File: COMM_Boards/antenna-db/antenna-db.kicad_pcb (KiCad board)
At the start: 4 copper layers, 95 x 95 mm, 65 parts, among them J1 Conn_01x03, J2 Conn_01x04, J3 Conn_01x02_Male, J6 Conn_01x02_Male, T1 MABA-007159-000000, T2 MABA-007159-000000, U1 SC4216HSETRT, U2 STM32F030CCT6, U3 SC4216HSETRT, U4 74AHC1G08, U5 74AHC1G08

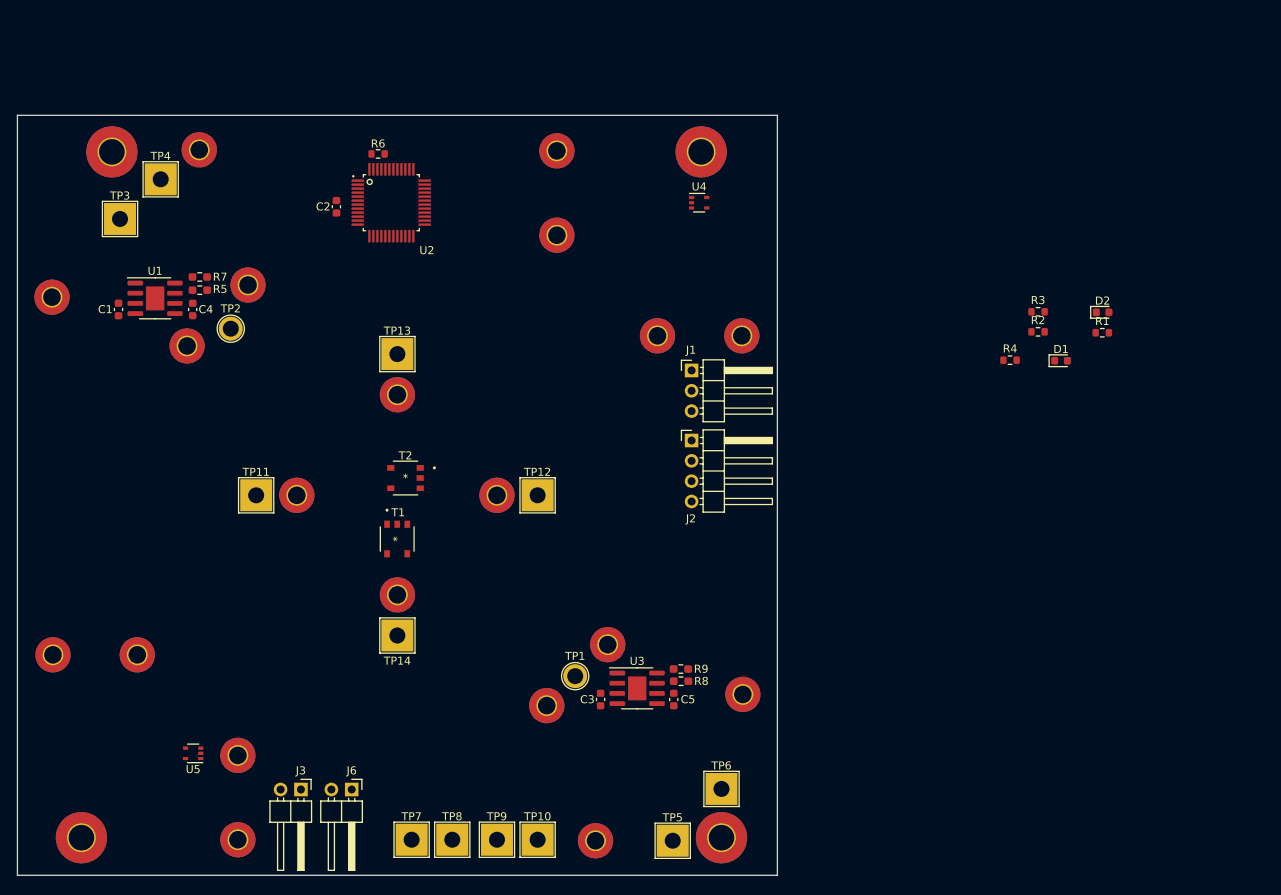
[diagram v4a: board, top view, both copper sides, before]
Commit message: finish layout of ANTT-DBD
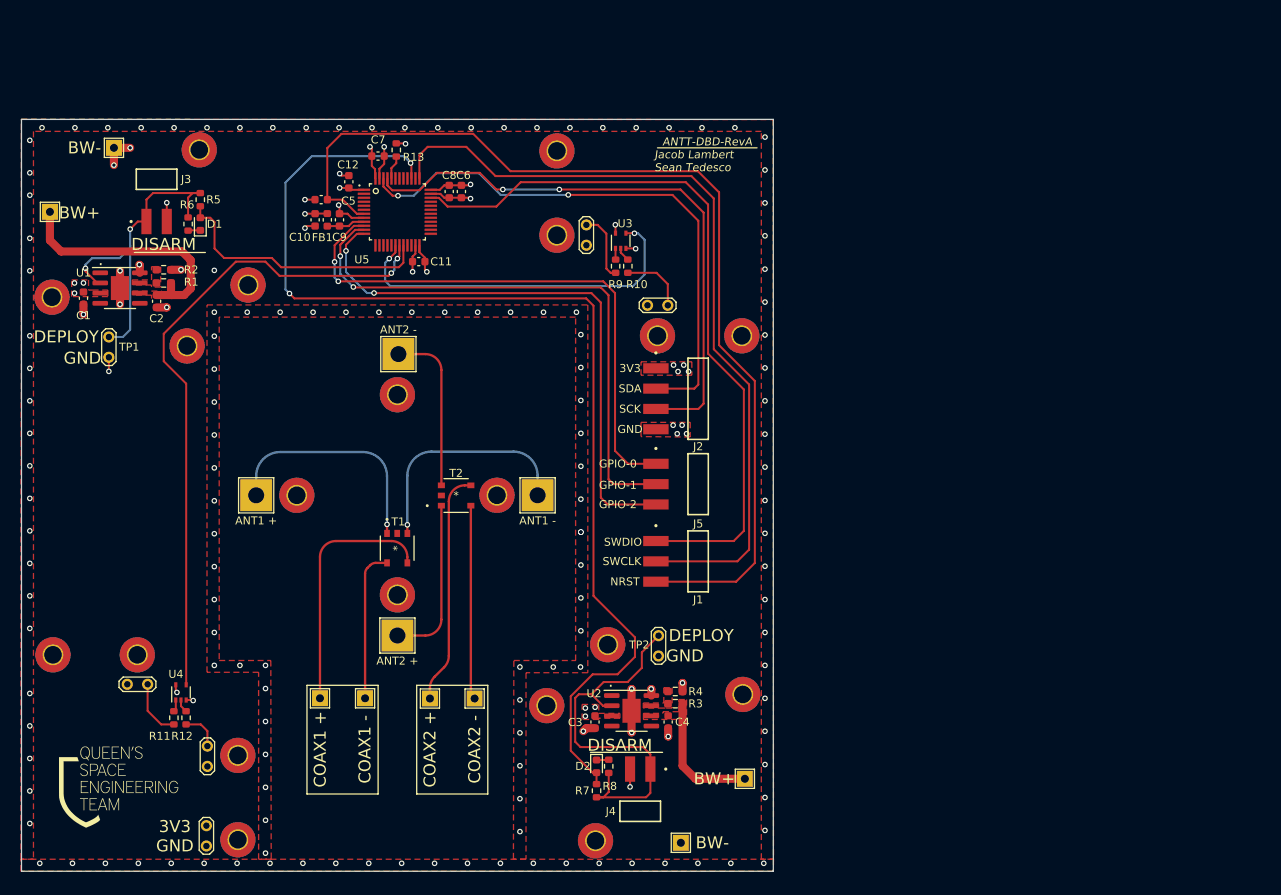
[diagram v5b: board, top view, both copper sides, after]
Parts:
- removed H1, H2, H3, H4: MountingHole_Pad, MountingHole:MountingHole_3.2mm_M3_Pad_TopBottom
- removed J6: Conn_01x02_Male, Connector_PinHeader_2.54mm:PinHeader_1x02_P2.54mm_Horizontal
- added C10: 10u, Capacitor_SMD:C_0603_1608Metric, F.Cu at (146.6, 60.9)
- added C11: 100n, Capacitor_SMD:C_0603_1608Metric, F.Cu at (159.5, 66.2)
- added C12: 100n, Capacitor_SMD:C_0603_1608Metric, F.Cu at (150.8, 56.2)
- added C6: 10u, Capacitor_SMD:C_0603_1608Metric, F.Cu at (164.8, 57.4)
- added C7: 100n, Capacitor_SMD:C_0603_1608Metric, F.Cu at (154.4, 53.0)
- added C8: 100n, Capacitor_SMD:C_0603_1608Metric, F.Cu at (163.3, 57.4)
- added C9: 100n, Capacitor_SMD:C_0603_1608Metric, F.Cu at (149.6, 60.9)
- added FB1: 100R @ 100M, Inductor_SMD:L_0603_1608Metric, F.Cu at (148.1, 60.9)
- added G***: LOGO, LOGO, F.Cu at (122.0, 131.7)
- added J4: Conn_01x02_Male, qset-footprints:SAMTEC_TSM-102-01-L-SH, F.Cu at (187.2, 134.9)
- added J5: Conn_01x03, qset-footprints:SAMTEC_TSM-103-01-L-SH, F.Cu at (194.4, 94.0)
- added R10: 0, Resistor_SMD:R_0603_1608Metric, F.Cu at (185.6, 66.7)
- added R11: 0, Resistor_SMD:R_0603_1608Metric, F.Cu at (128.9, 123.2)
- added R12: 0, Resistor_SMD:R_0603_1608Metric, F.Cu at (130.4, 123.2)
- added R9: 0, Resistor_SMD:R_0603_1608Metric, F.Cu at (184.1, 66.7)
- added TP3: Power Sensing, TestPoint:TestPoint_2Pads_Pitch2.54mm_Drill0.8mm, F.Cu at (133.0, 136.7)
- added TP4: TestPoint_2Pole, TestPoint:TestPoint_2Pads_Pitch2.54mm_Drill0.8mm, F.Cu at (180.5, 64.1)
- added TP5: TestPoint_2Pole, TestPoint:TestPoint_2Pads_Pitch2.54mm_Drill0.8mm, F.Cu at (188.1, 71.6)
- added TP6: TestPoint_2Pole, TestPoint:TestPoint_2Pads_Pitch2.54mm_Drill0.8mm, F.Cu at (123.1, 119.0)
- added TP7: TestPoint_2Pole, TestPoint:TestPoint_2Pads_Pitch2.54mm_Drill0.8mm, F.Cu at (133.1, 129.3)
- J1: footprint Connector_PinHeader_2.54mm:PinHeader_1x03_P2.54mm_Horizontal -> qset-footprints:SAMTEC_TSM-103-01-L-SH
- J2: footprint Connector_PinHeader_2.54mm:PinHeader_1x04_P2.54mm_Horizontal -> qset-footprints:SAMTEC_TSM-104-01-L-SH
- J3: footprint Connector_PinHeader_2.54mm:PinHeader_1x02_P2.54mm_Horizontal -> qset-footprints:SAMTEC_TSM-102-01-L-SH
- TP1: value PWR_EN_144 -> Manual Enable - 144 Deployment; footprint TestPoint:TestPoint_Plated_Hole_D2.0mm -> TestPoint:TestPoint_2Pads_Pitch2.54mm_Drill0.8mm
- TP10: renamed from TP11; value 144 Atenna Arm + -> ANT1 +
- TP11: renamed from TP12; value 144 Atenna Arm - -> ANT1 -
- TP12: renamed from TP9; footprint TestPoint:TestPoint_THTPad_4.0x4.0mm_Drill2.0mm -> TestPoint:TestPoint_THTPad_2.0x2.0mm_Drill1.0mm
- TP13: renamed from TP10; footprint TestPoint:TestPoint_THTPad_4.0x4.0mm_Drill2.0mm -> TestPoint:TestPoint_THTPad_2.0x2.0mm_Drill1.0mm
- TP14: renamed from TP13; value 434 Atenna Arm + -> ANT2 +
- TP15: renamed from TP14; value 434 Atenna Arm - -> ANT2 -
- TP16: renamed from TP3; value TestPoint -> 144 Burn Wire -; footprint TestPoint:TestPoint_THTPad_4.0x4.0mm_Drill2.0mm -> TestPoint:TestPoint_THTPad_2.0x2.0mm_Drill1.0mm
- TP17: renamed from TP4; value TestPoint -> 144 Burn Wire +; footprint TestPoint:TestPoint_THTPad_4.0x4.0mm_Drill2.0mm -> TestPoint:TestPoint_THTPad_2.0x2.0mm_Drill1.0mm
- TP18: renamed from TP5; value TestPoint -> 434 Burn Wire -; footprint TestPoint:TestPoint_THTPad_4.0x4.0mm_Drill2.0mm -> TestPoint:TestPoint_THTPad_2.0x2.0mm_Drill1.0mm
- TP19: renamed from TP6; value TestPoint -> 434 Burn Wire +; footprint TestPoint:TestPoint_THTPad_4.0x4.0mm_Drill2.0mm -> TestPoint:TestPoint_THTPad_2.0x2.0mm_Drill1.0mm
- TP2: value PWR_EN_144 -> Manual Enable - 434 Deployment; footprint TestPoint:TestPoint_Plated_Hole_D2.0mm -> TestPoint:TestPoint_2Pads_Pitch2.54mm_Drill0.8mm
- TP8: renamed from TP7; footprint TestPoint:TestPoint_THTPad_4.0x4.0mm_Drill2.0mm -> TestPoint:TestPoint_THTPad_2.0x2.0mm_Drill1.0mm
- TP9: renamed from TP8; footprint TestPoint:TestPoint_THTPad_4.0x4.0mm_Drill2.0mm -> TestPoint:TestPoint_THTPad_2.0x2.0mm_Drill1.0mm
- moved R6 115.1 mm to (130.7, 61.5), turned to 90 degrees
- moved D1 108.9 mm to (132.2, 61.5), turned to 90 degrees
- moved R5 105.7 mm to (132.2, 58.4), turned to 90 degrees
- moved D2 85.0 mm to (181.7, 129.3), turned to -90 degrees
- moved J3 78.4 mm to (126.7, 55.9), turned to 0 degrees
- moved R8 76.4 mm to (183.3, 129.3), turned to -90 degrees
- moved R7 74.6 mm to (181.7, 132.3), turned to -90 degrees
- moved TP1 72.1 mm to (120.8, 75.6), turned to -90 degrees
- moved TP2 65.8 mm to (189.5, 112.9), turned to -90 degrees
- moved TP15 35.2 mm to (157.0, 77.7)
- moved TP14 35.2 mm to (156.8, 112.9)
- moved TP9 24.2 mm to (147.2, 120.8)
- moved J1 23.9 mm to (194.4, 103.6), turned to -90 degrees
- moved TP13 22.2 mm to (160.9, 120.8)
- moved TP8 18.6 mm to (152.8, 120.8)
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- renumbered C4 to C2, C5 to C4, C2 to C5, R5 to R1, R6 to R13, R7 to R2, R8 to R3, R9 to R4, R3 to R5, R1 to R6, R4 to R7, R2 to R8, U3 to U2, U4 to U3, U5 to U4, U2 to U5
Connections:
- T1 pad 4: GND -> Net-(T1-Pad4)
- T2 pad 4: GND -> Net-(T2-Pad4)
- TP13 pad 1: GND -> Net-(T2-Pad4)
- TP2 pad 1: POWER_144_EN -> POWER_434_EN
- TP9 pad 1: GND -> Net-(T1-Pad4)
- U2 pad 2: POWER_144_EN -> POWER_434_EN
- U4 pad 4: DPY_DTC_144_GPIO_3V3 -> DPY_DTC_434_GPIO_3V3
- U5 pad 9: unconnected-(U2-Pad9) -> +3.3VA
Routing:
- net PWR_EN_434_3V3_GPIO: track 0.00 -> 140.7 mm, vias 0 -> 2
- net NRST: track 0.00 -> 126.4 mm
- net SWCLK: track 0.00 -> 100.8 mm
- net SWDIO: track 0.00 -> 91.7 mm
- net DPY_DTC_434_GPIO_3V3: track 0.00 -> 82.0 mm, vias 0 -> 2
- net I2C1-SCK: track 0.00 -> 73.7 mm, vias 0 -> 2
- net SYS-GPIO2: track 0.00 -> 71.3 mm, vias 0 -> 2
- net SYS-GPIO1: track 0.00 -> 71.2 mm, vias 0 -> 2
- net I2C1-SDA: track 0.00 -> 70.5 mm, vias 0 -> 2
- net SYS-GPIO0: track 0.00 -> 70.1 mm, vias 0 -> 2
- net GND: track 0.00 -> 54.0 mm, vias 0 -> 169
- net POWER_434_EN: track 0.00 -> 49.4 mm
- net DPY_DTC_144_GPIO_3V3: track 0.00 -> 45.3 mm, vias 0 -> 2
- net POWER_144_EN: track 0.00 -> 42.1 mm, vias 0 -> 2
- net PWR_EN_144_3V3_GPIO: track 0.00 -> 33.7 mm
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- added copper zone on F.Cu, net +3V3
- added copper zone on In2.Cu, net +3V3
- added copper zone on F.Cu, net GND
- added copper zone on In1.Cu, net GND
- added copper zone on F.Cu, net Net-(C2-Pad2)
- added copper zone on F.Cu, net Net-(C4-Pad2)
- added copper zone on F.Cu, net Net-(R1-Pad2)
- added copper zone on F.Cu, net Net-(R3-Pad2)
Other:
- board size 95 x 95 mm -> 94 x 94 mm
- board text added: "."
- board text added: "3V3"
- board text added: "ANTT-DBD-RevA"
- board text added: "BW+"
- board text added: "BW-"
- board text added: "COAX1 +"
- board text added: "COAX1 -"
- board text added: "COAX2 +"
- board text added: "COAX2 -"
- board text added: "DEPLOY"
- board text added: "DISARM"
- board text added: "GND"
- board text added: "GPIO-0"
- board text added: "GPIO-1"
- board text added: "GPIO-2"
- board text added: "Jacob Lambert Sean Tedesco"
- board text added: "NRST"
- board text added: "SCK"
- board text added: "SDA"
- board text added: "SWCLK"
- board text added: "SWDIO"

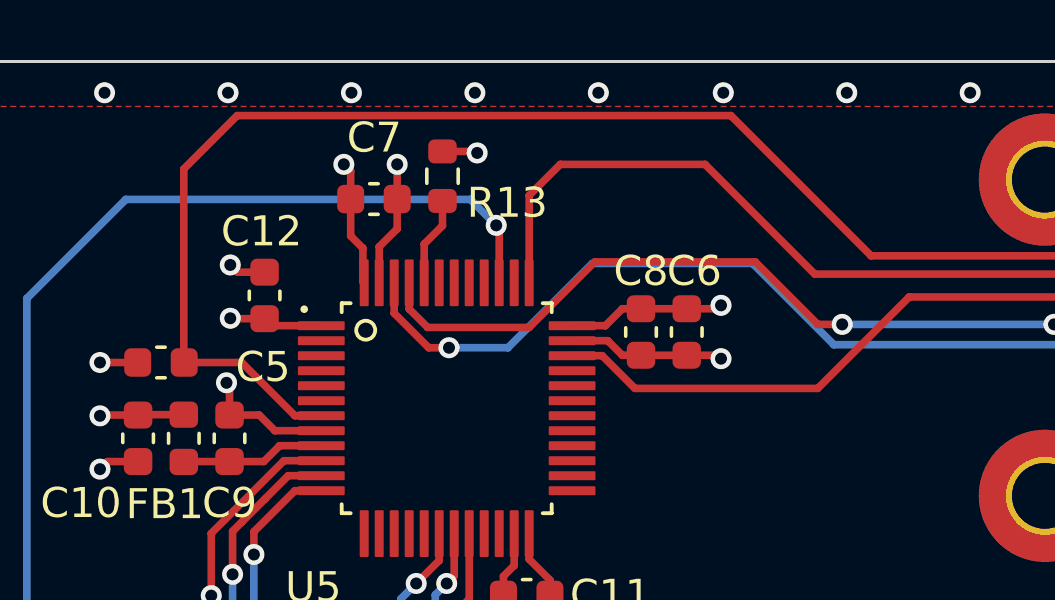
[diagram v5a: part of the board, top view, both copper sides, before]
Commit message: COMM: include manufacturing and assembly files
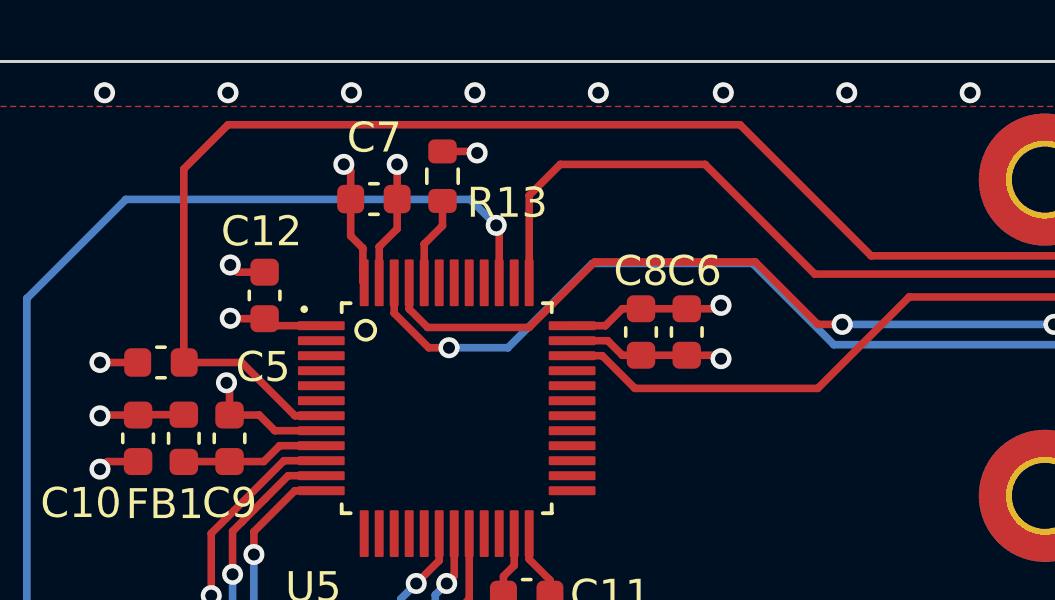
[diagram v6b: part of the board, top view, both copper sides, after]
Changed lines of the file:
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@@
       (layerselection 0x00010fc_ffffffff)
       (disableapertmacros false)
-      (usegerberextensions false)
+      (usegerberextensions true)
       (usegerberattributes true)
-      (usegerberadvancedattributes true)
-      (creategerberjobfile true)
+      (usegerberadvancedattributes false)
+      (creategerberjobfile false)
       (svguseinch false)
       (svgprecision 6)
@@
       (psa4output false)
       (plotreference true)
-      (plotvalue true)
+      (plotvalue false)
       (plotinvisibletext false)
       (sketchpadsonfab false)
-      (subtractmaskfromsilk false)
+      (subtractmaskfromsilk true)
       (outputformat 1)
       (mirror false)
-      (drillshape 1)
+      (drillshape 0)
       (scaleselection 1)
-      (outputdirectory "")
+      (outputdirectory "bill-of-material/")
     )
   )
@@
   (segment (start 193.5988 55.4736) (end 169.1132 55.4736) (width 0.254) (layer "F.Cu") (net 9))
   (segment (start 160.6296 51.816) (end 159.595 52.8506) (width 0.254) (layer "F.Cu") (net 9))
-  (segment (start 166.3192 50.1904) (end 149.86 50.1904) (width 0.254) (layer "F.Cu") (net 10))
-  (segment (start 148.082 58.661) (end 148.095 58.674) (width 0.254) (layer "F.Cu") (net 10))
+  (segment (start 201.5236 81.0768) (end 197.0532 76.6064) (width 0.254) (layer "F.Cu") (net 10))
+  (segment (start 189.157 106.172) (end 199.1868 106.172) (width 0.254) (layer "F.Cu") (net 10))
+  (segment (start 170.9928 54.864) (end 166.624 50.4952) (width 0.254) (layer "F.Cu") (net 10))
   (segment (start 201.5236 103.8352) (end 201.5236 81.0768) (width 0.254) (layer "F.Cu") (net 10))
-  (segment (start 197.0532 57.5056) (end 194.4116 54.864) (width 0.254) (layer "F.Cu") (net 10))
-  (segment (start 197.0532 76.6064) (end 197.0532 57.5056) (width 0.254) (layer "F.Cu") (net 10))
-  (segment (start 148.349 58.42) (end 148.095 58.674) (width 0.254) (layer "F.Cu") (net 10))
-  (segment (start 199.1868 106.172) (end 201.5236 103.8352) (width 0.254) (layer "F.Cu") (net 10))
+  (segment (start 148.349 58.42) (end 150.0124 58.42) (width 0.254) (layer "F.Cu") (net 10))
   (segment (start 194.4116 54.864) (end 170.9928 54.864) (width 0.254) (layer "F.Cu") (net 10))
-  (segment (start 150.0124 58.42) (end 148.349 58.42) (width 0.254) (layer "F.Cu") (net 10))
-  (segment (start 151.7864 60.194) (end 150.0124 58.42) (width 0.254) (layer "F.Cu") (net 10))
-  (segment (start 170.9928 54.864) (end 166.3192 50.1904) (width 0.254) (layer "F.Cu") (net 10))
-  (segment (start 201.5236 81.0768) (end 197.0532 76.6064) (width 0.254) (layer "F.Cu") (net 10))
-  (segment (start 152.665 60.194) (end 151.7864 60.194) (width 0.254) (layer "F.Cu") (net 10))
+  (segment (start 149.5552 50.4952) (end 148.082 51.9684) (width 0.254) (layer "F.Cu") (net 10))
+  (segment (start 197.0532 76.6064) (end 197.0532 57.5056) (width 0.254) (layer "F.Cu") (net 10))
   (segment (start 148.082 51.9684) (end 148.082 58.661) (width 0.254) (layer "F.Cu") (net 10))
-  (segment (start 189.157 106.172) (end 199.1868 106.172) (width 0.254) (layer "F.Cu") (net 10))
-  (segment (start 149.86 50.1904) (end 148.082 51.9684) (width 0.254) (layer "F.Cu") (net 10))
+  (segment (start 197.0532 57.5056) (end 194.4116 54.864) (width 0.254) (layer "F.Cu") (net 10))
+  (segment (start 199.1868 106.172) (end 201.5236 103.8352) (width 0.254) (layer "F.Cu") (net 10))
+  (segment (start 151.7864 60.194) (end 152.665 60.194) (width 0.254) (layer "F.Cu") (net 10))
+  (segment (start 148.082 58.661) (end 148.095 58.674) (width 0.254) (layer "F.Cu") (net 10))
+  (segment (start 166.624 50.4952) (end 149.5552 50.4952) (width 0.254) (layer "F.Cu") (net 10))
+  (segment (start 150.0124 58.42) (end 151.7864 60.194) (width 0.254) (layer "F.Cu") (net 10))
+  (segment (start 148.095 58.674) (end 148.349 58.42) (width 0.254) (layer "F.Cu") (net 10))
   (segment (start 145.314 60.172) (end 145.288 60.198) (width 0.254) (layer "F.Cu") (net 11))
   (segment (start 160.287 65.672) (end 160.287 66.167) (width 0.254) (layer "F.Cu") (net 11))
